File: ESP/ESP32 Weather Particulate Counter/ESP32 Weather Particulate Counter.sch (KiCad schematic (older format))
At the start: 75 parts, among them J1 Conn_01x02, J10 WIND, J11 Conn_01x05, J2 Conn_01x05, J3 Conn_01x01, J4 Conn_01x01, J5 Conn_01x08, J6 Conn_01x08, J7 Conn_01x04, J8 Conn_01x04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

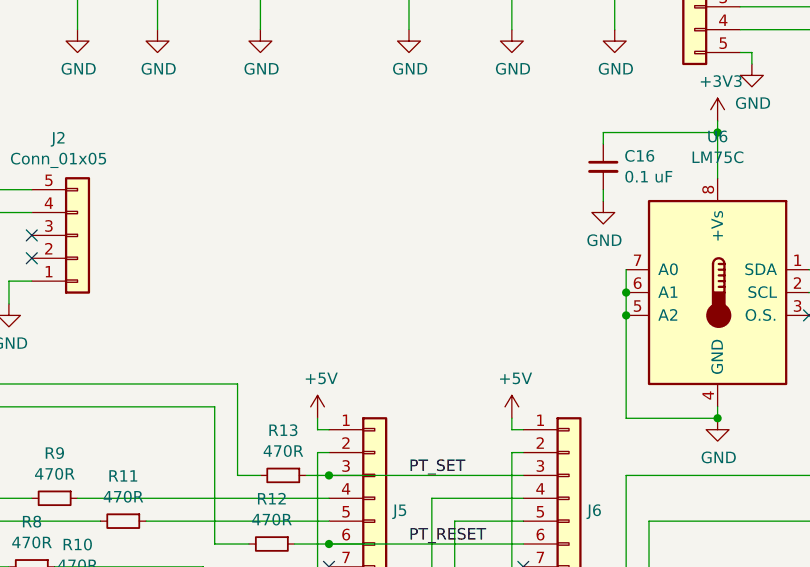
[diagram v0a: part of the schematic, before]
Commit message: Second rev. There were issues: Meter Monitor:  - CH340 has strange connection issues. I think that 3.3V operation mode is either problematic or there's stuff you need to do that's not in the datasheet. ESP32-CAM PSU:  - Camera connections are on 0.075" centers, not 0.1" centers. WTF? How did I even do that? Particulate counter:  - Plantower numbers their interface connector from the wrong end. I made crossover cables, but the connectors could also just be installed backwards.
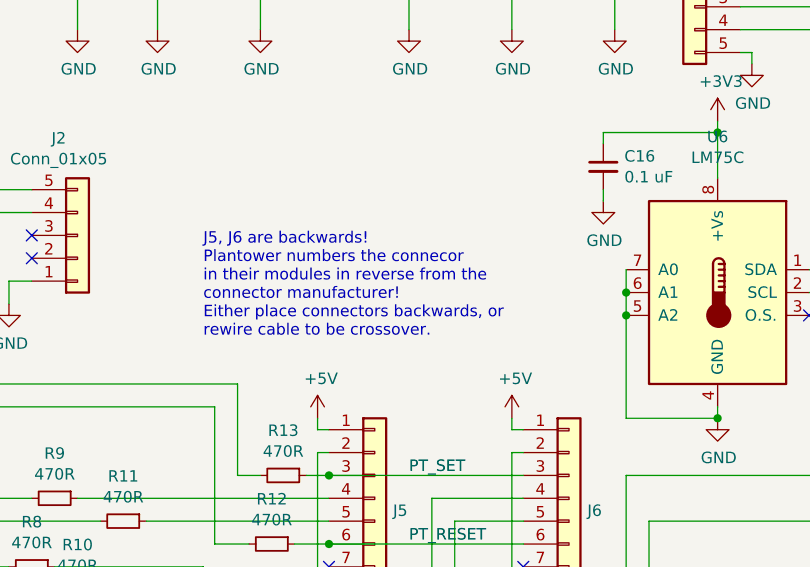
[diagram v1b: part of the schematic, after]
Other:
- note added: "J5, J6 are backwards!\nPlantower numbers the connecor \nin their modules in reverse from the \nconnector manufacturer!\nEither place connectors backwards, or \nrewire cable to be crossover."
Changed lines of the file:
@@
 NoConn ~ 1550 3250
 NoConn ~ 8300 3050
+Text Notes 5650 3150 0    50   ~ 0
+J5, J6 are backwards!\nPlantower numbers the connecor \nin their modules in reverse from the \nconnector manufacturer!\nEither place connectors backwards, or \nrewire cable to be crossover.
 $EndSCHEMATC

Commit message: More eratta. Ugh.
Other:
- note added: "R19 breaks boot (it switches the \nflash to 1.8V mode by pulling GPIO12 \nhigh at boot).\nRemove R19 and do not use J8"
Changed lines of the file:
@@
 Text Notes 5650 3150 0    50   ~ 0
 J5, J6 are backwards!\nPlantower numbers the connecor \nin their modules in reverse from the \nconnector manufacturer!\nEither place connectors backwards, or \nrewire cable to be crossover.
+Text Notes 7800 4800 0    50   ~ 0
+R19 breaks boot (it switches the \nflash to 1.8V mode by pulling GPIO12 \nhigh at boot).\nRemove R19 and do not use J8
 $EndSCHEMATC
